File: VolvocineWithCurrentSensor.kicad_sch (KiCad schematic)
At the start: 14 parts, among them J2 Conn_01x12_Socket, J3 Sensors, J4 Switch, J5 battery, J6 Conn_01x12_Socket, U1 PAM2401SCADJ, U3 INA226

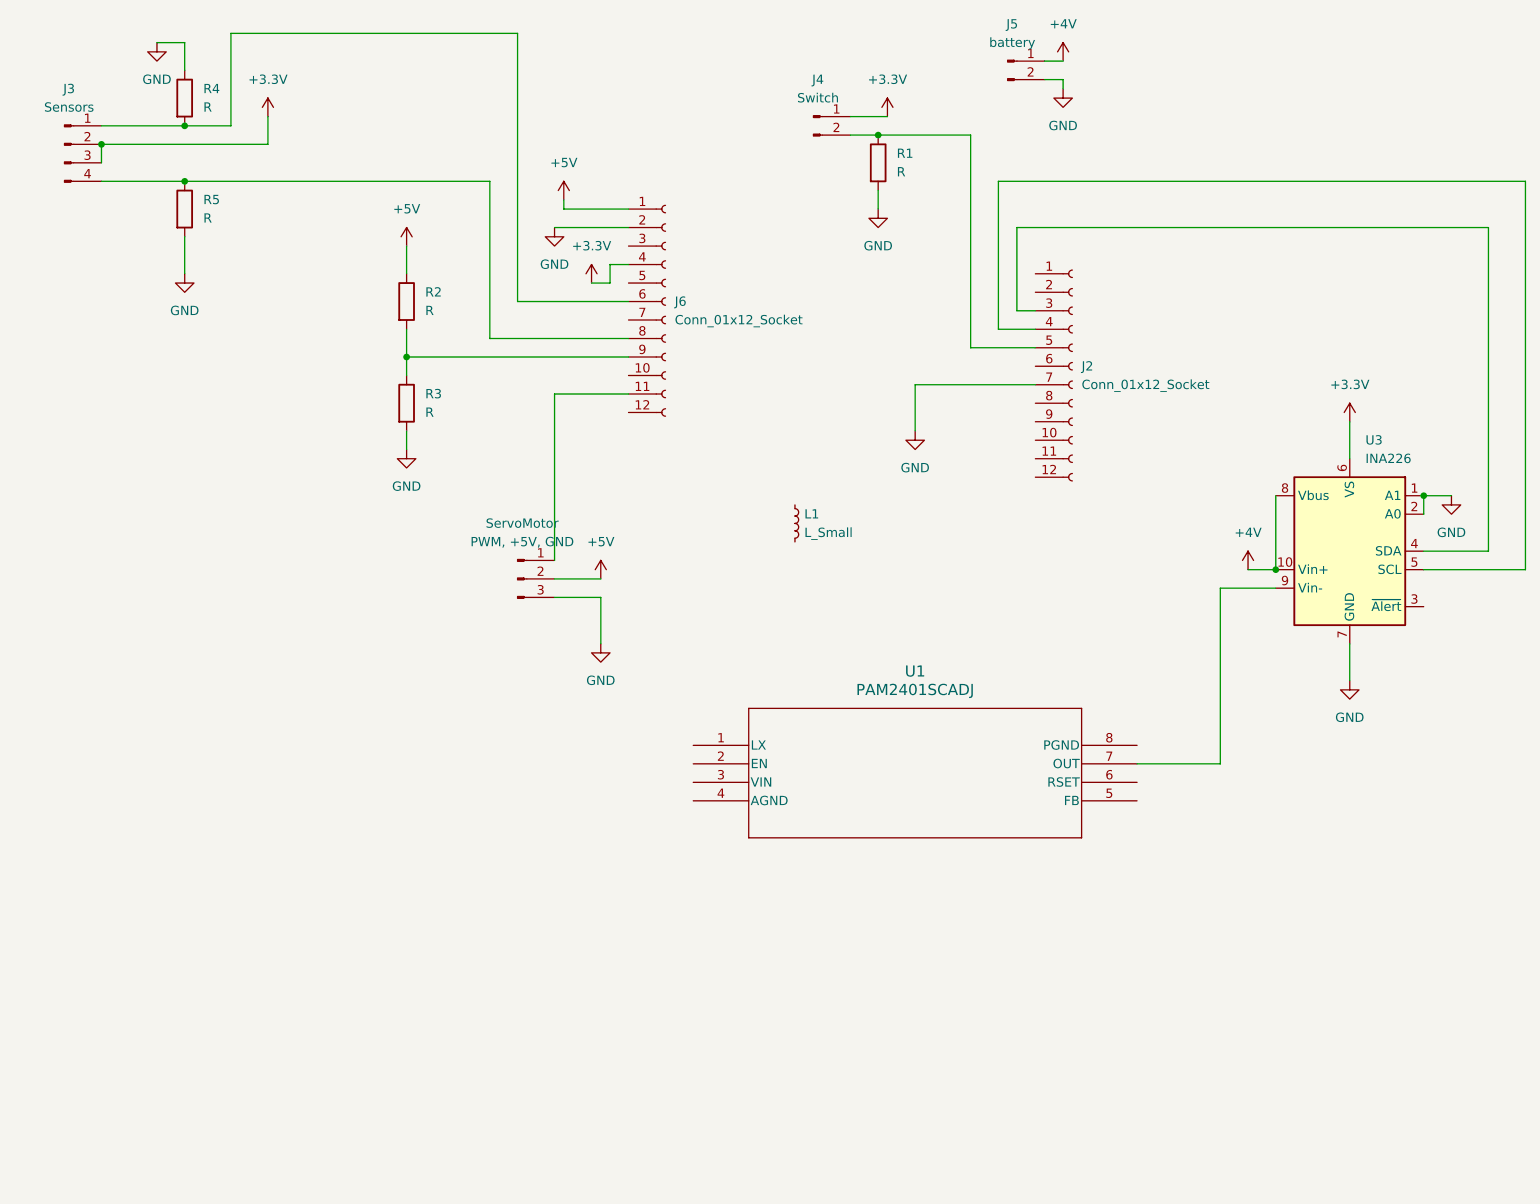
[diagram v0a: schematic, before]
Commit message: Add Gerber and drill files for VolvocineWithCurrentSensor project
- Created NPTH drill file for non-plated holes.
- Created PTH drill file for plated through holes with detailed coordinates.
- Added job file containing project metadata and file attributes for Gerber outputs.
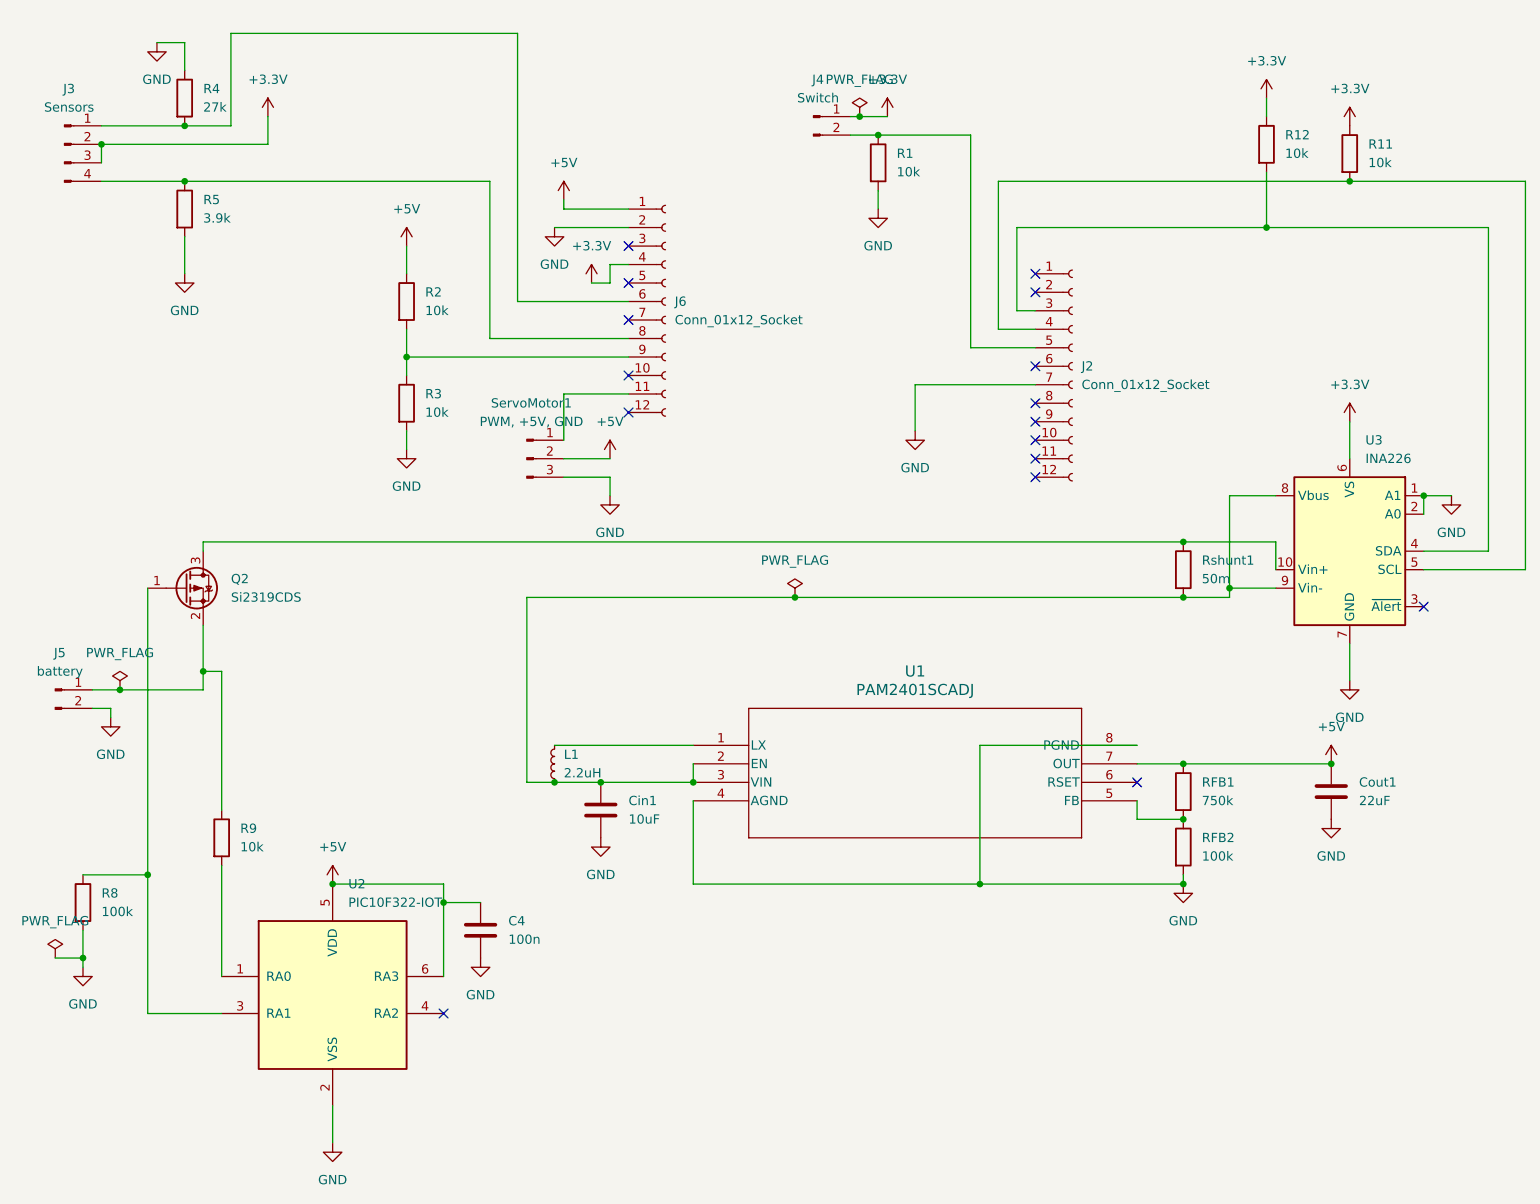
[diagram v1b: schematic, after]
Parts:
- added C4: 100n, Capacitor_SMD:C_0603_1608Metric_Pad1.08x0.95mm_HandSolder, symbol Device:C
- added Cin1: 10uF, Capacitor_SMD:C_0603_1608Metric_Pad1.08x0.95mm_HandSolder, symbol Device:C
- added Cout1: 22uF, Capacitor_SMD:C_1206_3216Metric_Pad1.33x1.80mm_HandSolder, symbol Device:C
- added Q2: Si2319CDS, Package_TO_SOT_SMD:SOT-23, symbol Transistor_FET:Si2319CDS
- added R11, R12, R9: 10k, Resistor_SMD:R_0603_1608Metric_Pad0.98x0.95mm_HandSolder, symbol Device:R
- added R8, RFB2: 100k, Resistor_SMD:R_0603_1608Metric_Pad0.98x0.95mm_HandSolder, symbol Device:R
- added RFB1: 750k, Resistor_SMD:R_0603_1608Metric_Pad0.98x0.95mm_HandSolder, symbol Device:R
- added Rshunt1: 50m, Resistor_SMD:R_1206_3216Metric_Pad1.30x1.75mm_HandSolder, symbol Device:R
- added U2: PIC10F322-IOT, Package_TO_SOT_SMD:SOT-23-6, symbol MCU_Microchip_PIC10:PIC10F322-IOT
- J2, J6: footprint (none) -> Connector_PinSocket_2.54mm:PinSocket_1x12_P2.54mm_Vertical
- J3: footprint (none) -> Connector_PinHeader_2.54mm:PinHeader_1x04_P2.54mm_Horizontal
- J4, J5: footprint (none) -> Connector_PinHeader_2.54mm:PinHeader_1x02_P2.54mm_Horizontal
- L1: value L_Small -> 2.2uH; footprint (none) -> Inductor_SMD:L_1008_2520Metric_Pad1.43x2.20mm_HandSolder
- R1, R2, R3: value R -> 10k; footprint (none) -> Resistor_SMD:R_0603_1608Metric_Pad0.98x0.95mm_HandSolder
- R4: value R -> 27k; footprint (none) -> Resistor_SMD:R_0603_1608Metric_Pad0.98x0.95mm_HandSolder
- R5: value R -> 3.9k; footprint (none) -> Resistor_SMD:R_0603_1608Metric_Pad0.98x0.95mm_HandSolder
- ServoMotor1: renamed from ServoMotor; footprint (none) -> Connector_PinHeader_2.54mm:PinHeader_1x03_P2.54mm_Horizontal
- U1: footprint MSOP8_DIO -> Package_SO:MSOP-8_3x3mm_P0.65mm
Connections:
- net +3.3V: now also R11.1, R12.1
- net +5V: now also U1.7 (OUT), C4.1, Cout1.1, RFB1.1, U2.5 (VDD), U2.6 (RA3)
- net GND: now also U1.4 (AGND), U1.8 (PGND), C4.2, Cin1.2, Cout1.2, R8.2, RFB2.2, U2.2 (VSS)
- net at J2.3 (Pin_3), U3.4 (SDA): now also R12.2
- net at J2.4 (Pin_4), U3.5 (SCL): now also R11.2
- net at U3.9 (Vin-): now also L1.1, U1.2 (EN), U1.3 (VIN), U3.8 (Vbus), Cin1.1, Rshunt1.2; no longer U1.7 (OUT)
- net at U1.1 (LX): now also L1.2
- net at U1.5 (FB): now also RFB1.2, RFB2.1
- removed net +4V: J5.1 (Pin_1), U3.10 (Vin+), U3.8 (Vbus)
- new net: Q2.3 (D), Rshunt1.1, U3.10 (Vin+)
- new net: J5.1 (Pin_1), Q2.2 (S), R9.1
- new net: R9.2, U2.1 (RA0)
- new net: Q2.1 (G), R8.1, U2.3 (RA1)
- no-connect marks 0 -> 16
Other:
- moved on the sheet: J5, L1, ServoMotor1
